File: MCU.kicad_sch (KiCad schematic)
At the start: 23 parts, among them J11 Conn_01x03, J7 Conn_ST_STDC14, J8 Conn_01x03, J9 Conn_01x04, U16 STM32F303RETx

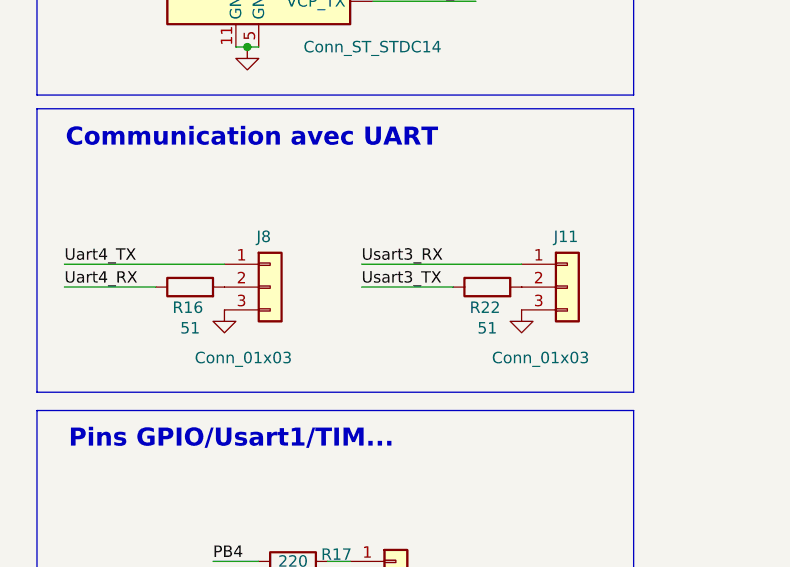
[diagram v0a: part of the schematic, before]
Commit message: alignement connecteur, changement connecteur
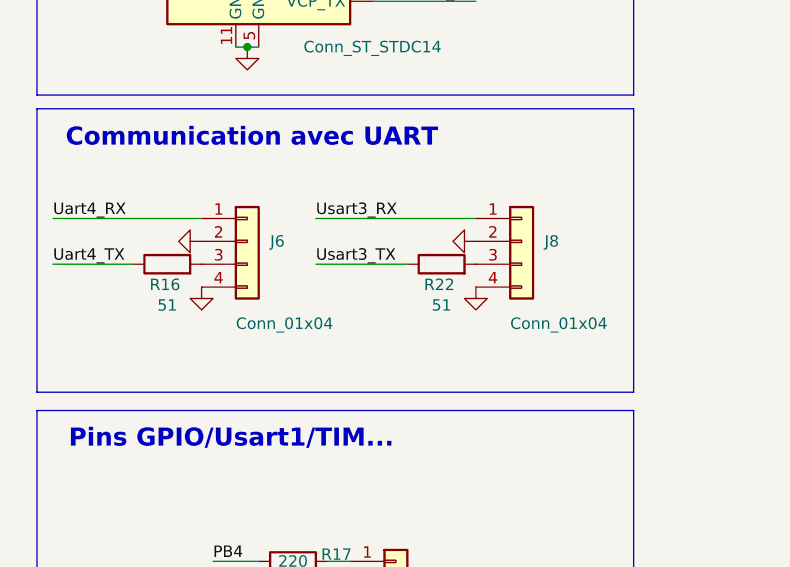
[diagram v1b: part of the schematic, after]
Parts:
- removed J11, J8: Conn_01x03, Connector_JST:JST_EH_B3B-EH-A_1x03_P2.50mm_Vertical, symbol Connector_Generic:Conn_01x03
- added J6, J8: Conn_01x04, Connector_JST:JST_EH_B4B-EH-A_1x04_P2.50mm_Vertical, symbol Connector_Generic:Conn_01x04
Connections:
- net GND: now also J6.2 (Pin_2), J6.4 (Pin_4), J8.2 (Pin_2), J8.4 (Pin_4)
- net Uart4_RX: now also J6.1 (Pin_1); no longer R16.1
- net Uart4_TX: now also R16.1
- net Usart3_RX: now also J8.1 (Pin_1)
- net at R22.2: now also J8.3 (Pin_3)
- net at R16.2: now also J6.3 (Pin_3)
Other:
- moved on the sheet: R16, R22

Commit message: final push
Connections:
- net USART2_RX: now also J7.13 (VCP_RX); no longer J7.14 (VCP_TX)
- net USART2_TX: now also J7.14 (VCP_TX); no longer J7.13 (VCP_RX)
- net GPIO_PB2: now reaches U16.28 (PB2)
- net GPIO_PB10: now reaches U16.29 (PB10)
- no-connect marks 27 -> 25
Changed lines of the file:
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@@
+	)
+	(no_connect
+		(at 189.23 105.41)
+	)
+	(no_connect
+		(at 189.23 82.55)
+	)
+	(no_connect
+		(at 189.23 54.61)
+	)
+	(no_connect
+		(at 189.23 62.23)
+	)
+	(no_connect
+		(at 153.67 62.23)
+	)
+	(no_connect
+		(at 189.23 57.15)
+	)
+	(no_connect
+		(at 153.67 80.01)
 	)
 	(no_connect
 		(at 189.23 102.87)
-	)
-	(no_connect
-		(at 189.23 105.41)
-	)
-	(no_connect
-		(at 189.23 82.55)
-	)
-	(no_connect
-		(at 189.23 54.61)
-	)
-	(no_connect
-		(at 189.23 113.03)
-	)
-	(no_connect
-		(at 189.23 92.71)
-	)
-	(no_connect
-		(at 189.23 62.23)
-	)
-	(no_connect
-		(at 153.67 62.23)
-	)
-	(no_connect
-		(at 189.23 57.15)
-	)
-	(no_connect
-		(at 153.67 80.01)
 	)
 	(no_connect
@@
 	)
 	(label "USART2_RX"
-		(at 77.47 71.12 180)
+		(at 77.47 68.58 180)
 		(effects
 			(font
@@
 	)
 	(label "USART2_TX"
-		(at 77.47 68.58 180)
+		(at 77.47 71.12 180)
 		(effects
 			(font
@@
 		)
 	)
+	(hierarchical_label "GPIO_PB2"
+		(shape input)
+		(at 189.23 92.71 0)
+		(effects
+			(font
+				(size 1.27 1.27)
+			)
+			(justify left)
+		)
+	)
 	(hierarchical_label "R_PWM"
 		(shape input)
@@
 		(effects
 			(font
+				(size 1.27 1.27)
+			)
+			(justify left)
+		)
+	)
+	(hierarchical_label "GPIO_PB10"
+		(shape input)
+		(at 189.23 113.03 0)
+		(effects
+			(font

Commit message: last push
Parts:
- U17: footprint Oscillator:WE-XTAL Quartz Crystal 8MHz -> Crystal:Crystal_SMD_7050-4Pin_7.0x5.0mm
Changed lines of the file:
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@@
 			)
 		)
-		(property "Footprint" "Oscillator:WE-XTAL Quartz Crystal 8MHz"
+		(property "Footprint" "Crystal:Crystal_SMD_7050-4Pin_7.0x5.0mm"
 			(at 245.11 82.55 0)
 			(effects
